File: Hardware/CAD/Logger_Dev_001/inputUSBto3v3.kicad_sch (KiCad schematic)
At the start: 30 parts, among them J4 Connector, USB-TYPE-C-16P, Q1 BC847BS, U5 AMS1117, U6 CP2102-GMR

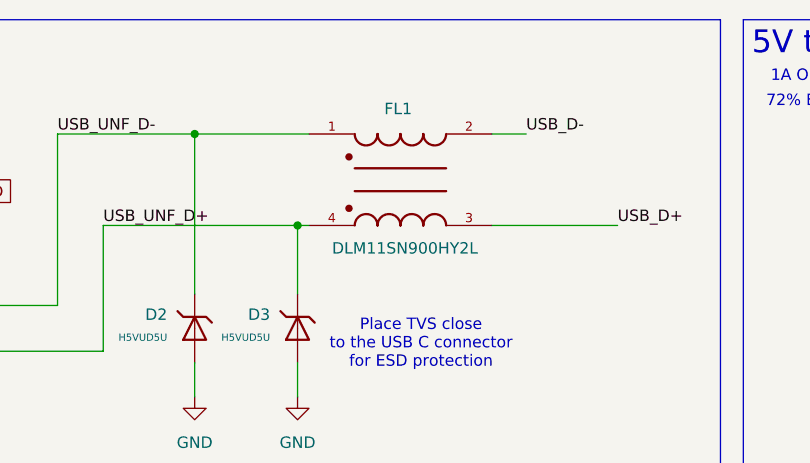
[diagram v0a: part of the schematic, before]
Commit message: Updated PCB to include strapping pin and USB C DP reroute
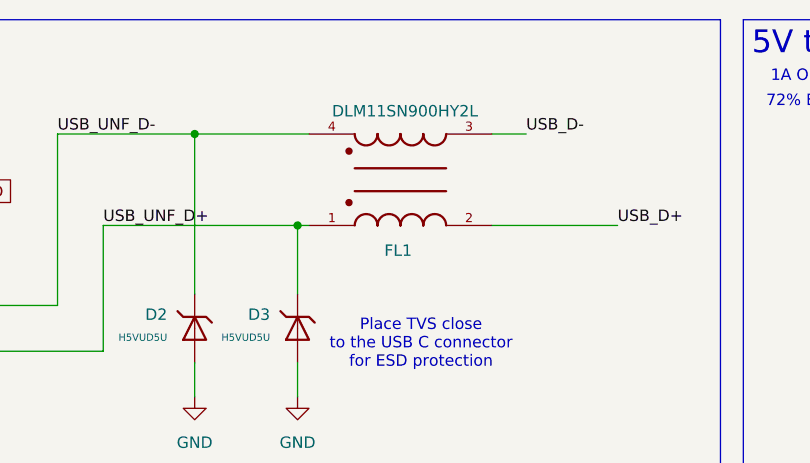
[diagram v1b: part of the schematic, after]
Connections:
- net USB_D+: now also FL1.2; no longer FL1.3
- net USB_D-: now also FL1.3; no longer FL1.2
- net USB_UNF_D+: now also FL1.1; no longer FL1.4
- net USB_UNF_D-: now also FL1.4; no longer FL1.1
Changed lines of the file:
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@@
 		(lib_id "DLM11SN900HY2L:DLM11SN900HY2L")
 		(at 119.38 33.02 0)
+		(mirror x)
 		(unit 1)
 		(exclude_from_sim no)
@@
 		(dnp no)
 		(property "Reference" "FL1"
-			(at 119.126 25.146 0)
+			(at 119.126 40.894 0)
 			(effects
 				(font
@@
 		)
 		(property "Value" "DLM11SN900HY2L"
-			(at 119.888 40.64 0)
+			(at 119.888 25.4 0)
 			(effects
 				(font
